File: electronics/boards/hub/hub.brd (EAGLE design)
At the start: 48 x 48 mm, 8 parts, among them J1 GROVE_CONNECTOR2.0_1X4, J2 GROVE_CONNECTOR2.0_1X4, J3 GROVE_CONNECTOR2.0_1X4, J4 GROVE_CONNECTOR2.0_1X4, J5 GROVE_CONNECTOR2.0_1X4, J6 GROVE_CONNECTOR2.0_1X4, J7 GROVE_CONNECTOR2.0_1X4, J8 GROVE_CONNECTOR2.0_1X4

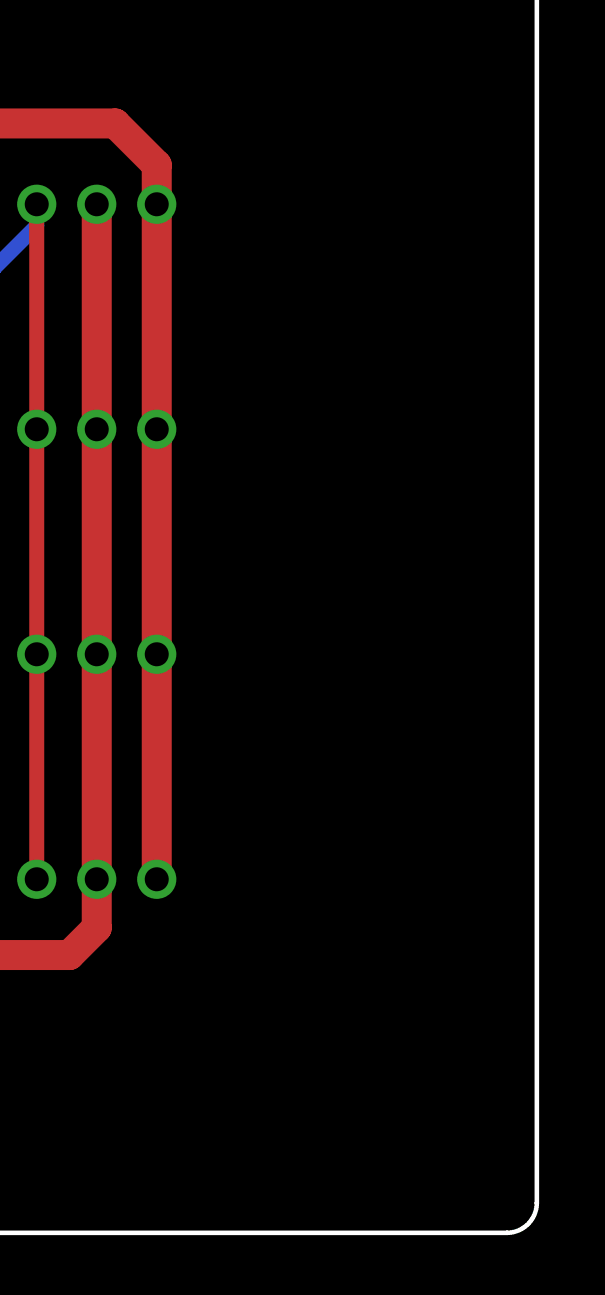
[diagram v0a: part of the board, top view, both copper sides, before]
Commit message: Logo hinzugefügt
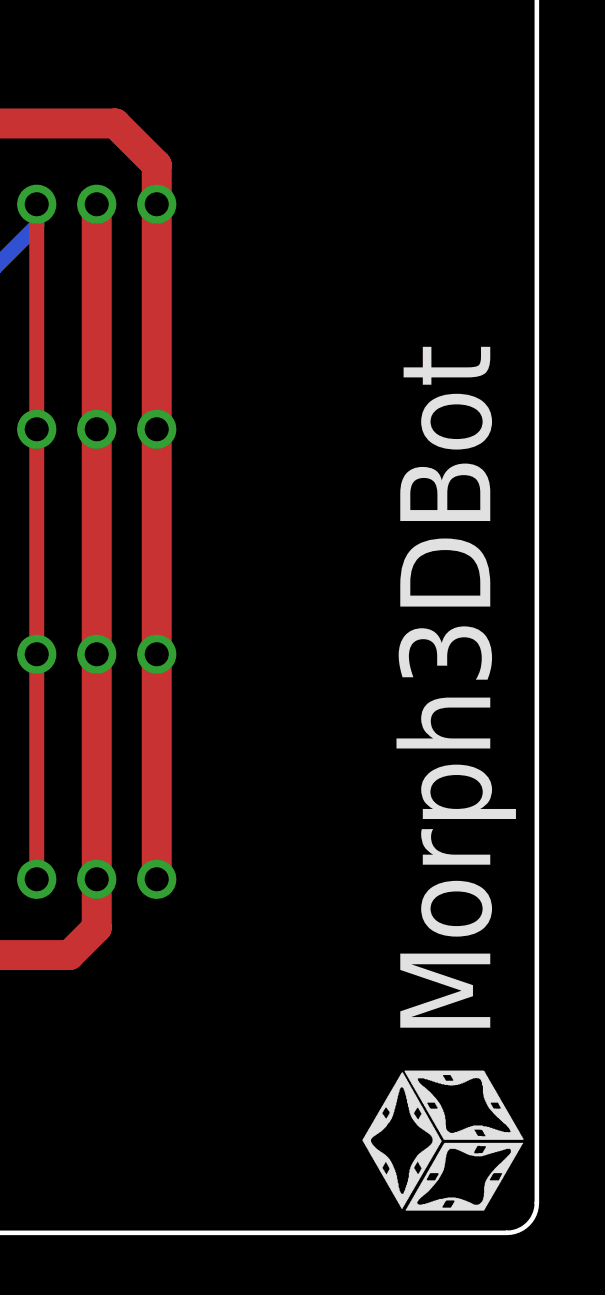
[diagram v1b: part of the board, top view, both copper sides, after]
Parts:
- added U$1: LOGO_MORPHBOT5MM, topo-eng:LOGO_MORPHBOT
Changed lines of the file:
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@@
 <layer number="104" name="Name" color="7" fill="1" visible="no" active="yes"/>
 <layer number="116" name="Patch_BOT" color="9" fill="4" visible="no" active="yes"/>
+<layer number="120" name="brd_placement_notes" color="7" fill="1" visible="yes" active="yes"/>
 <layer number="121" name="_tsilk" color="7" fill="1" visible="no" active="yes"/>
 <layer number="122" name="_bsilk" color="7" fill="1" visible="no" active="yes"/>
+<layer number="144" name="DrillLegend" color="7" fill="1" visible="yes" active="yes"/>
+<layer number="145" name="DrillLegend_01-16" color="7" fill="1" visible="yes" active="yes"/>
+<layer number="146" name="DrillLegend_01-20" color="7" fill="1" visible="yes" active="yes"/>
 <layer number="151" name="HeatSink" color="14" fill="1" visible="no" active="no"/>
+<layer number="198" name="BMP198" color="7" fill="1" visible="yes" active="yes"/>
+<layer number="199" name="Contour" color="7" fill="1" visible="yes" active="yes"/>
 <layer number="200" name="200bmp" color="1" fill="10" visible="no" active="no"/>
 <layer number="201" name="201bmp" color="2" fill="1" visible="no" active="no"/>
@@
 <layer number="207" name="207bmp" color="15" fill="10" visible="no" active="no"/>
 <layer number="208" name="208bmp" color="9" fill="10" visible="no" active="yes"/>
+<layer number="209" name="Route9Document" color="7" fill="1" visible="yes" active="yes"/>
+<layer number="210" name="Route10Document" color="7" fill="1" visible="yes" active="yes"/>
+<layer number="211" name="Route11Document" color="7" fill="1" visible="yes" active="yes"/>
+<layer number="212" name="Route12Document" color="7" fill="1" visible="yes" active="yes"/>
+<layer number="213" name="Route13Document" color="7" fill="1" visible="yes" active="yes"/>
+<layer number="214" name="Route14Document" color="7" fill="1" visible="yes" active="yes"/>
+<layer number="215" name="Route15Document" color="7" fill="1" visible="yes" active="yes"/>
+<layer number="216" name="BottomDocument" color="7" fill="1" visible="yes" active="yes"/>
+<layer number="220" name="DimensionDocument" color="7" fill="1" visible="yes" active="yes"/>
+<layer number="221" name="tPlaceDocument" color="7" fill="1" visible="yes" active="yes"/>
+<layer number="222" name="bPlaceDocument" color="7" fill="1" visible="yes" active="yes"/>
+<layer number="225" name="tNamesDocument" color="7" fill="1" visible="yes" active="yes"/>
+<layer number="226" name="bNamesDocument" color="7" fill="1" visible="yes" active="yes"/>
+<layer number="227" name="tValuesDocument" color="7" fill="1" visible="yes" active="yes"/>
+<layer number="228" name="bValuesDocument" color="7" fill="1" visible="yes" active="yes"/>
+<layer number="229" name="tStopDocument" color="7" fill="1" visible="yes" active="yes"/>
+<layer number="230" name="bStopDocument" color="7" fill="1" visible="yes" active="yes"/>
+<layer number="231" name="tCreamDocument" color="7" fill="1" visible="yes" active="yes"/>
+<layer number="232" name="bCreamDocument" color="7" fill="1" visible="yes" active="yes"/>
+<layer number="233" name="tFinishDocument" color="7" fill="1" visible="yes" active="yes"/>
+<layer number="234" name="bFinishDocument" color="7" fill="1" visible="yes" active="yes"/>
+<layer number="235" name="tGlueDocument" color="7" fill="1" visible="yes" active="yes"/>
+<layer number="236" name="bGlueDocument" color="7" fill="1" visible="yes" active="yes"/>
+<layer number="244" name="DrillsDocument" color="7" fill="1" visible="yes" active="yes"/>
+<layer number="245" name="HolesDocument" color="7" fill="1" visible="yes" active="yes"/>
+<layer number="246" name="MillingDocument" color="7" fill="1" visible="yes" active="yes"/>
+<layer number="247" name="MeasuresDocument" color="7" fill="1" visible="yes" active="yes"/>
 <layer number="250" name="Descript" color="3" fill="1" visible="no" active="no"/>
 <layer number="251" name="SMDround" color="12" fill="11" visible="no" active="no"/>
@@
 <attribute name="NAME" x="10.892778125" y="24.20470625" size="0.8128" layer="26" font="vector" ratio="10" rot="MR180"/>
 </element>
+<element name="U$1" library="topo-eng" library_urn="urn:adsk.eagle:library:6646478" package="LOGO_MORPHBOT" value="LOGO_MORPHBOT5MM" x="47.657946875" y="0.4947" smashed="yes" rot="R90"/>
 </elements>
 <signals>
@@
 </drawing>
 <compatibility>
+<note version="8.2" severity="warning">
+Since Version 8.2, EAGLE supports online libraries. The ids
+of those online libraries will not be understood (or retained)
+with this version.
+</note>
 <note version="8.3" severity="warning">
 Since Version 8.3, EAGLE supports URNs for individual library

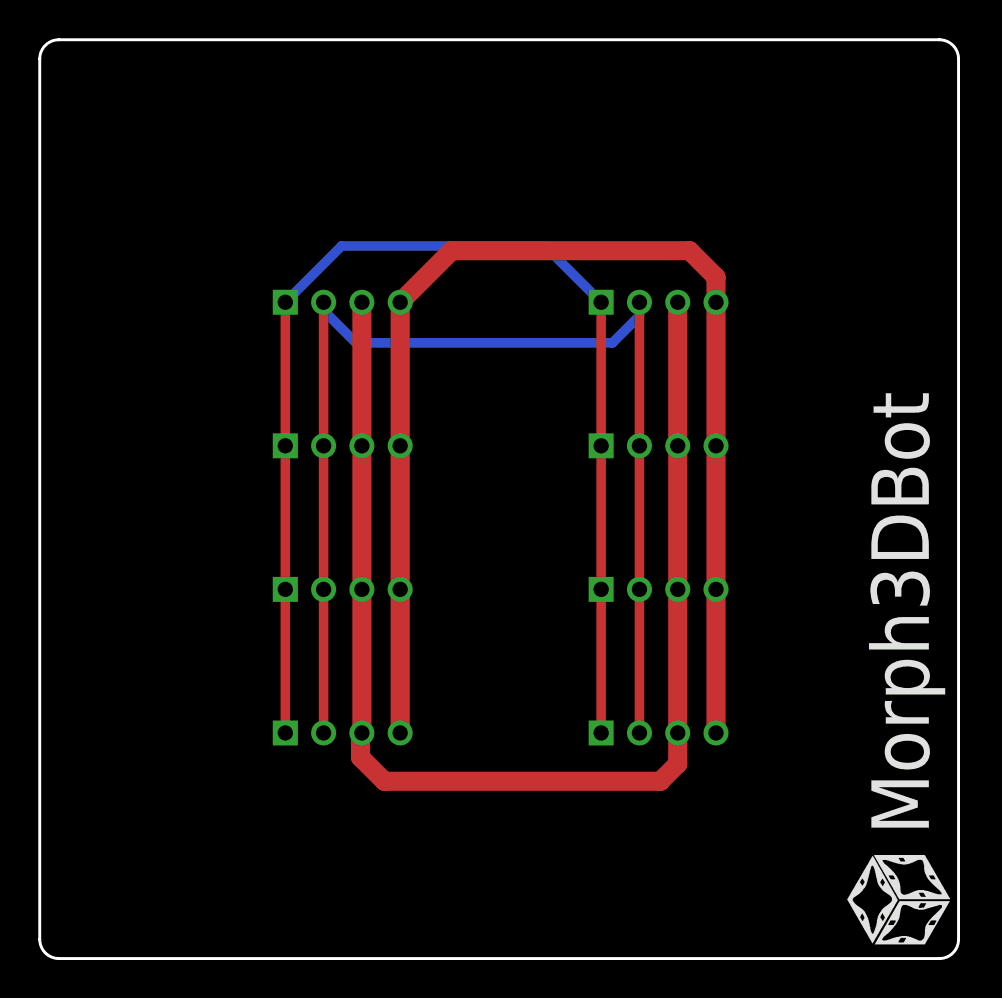
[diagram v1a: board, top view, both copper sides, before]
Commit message: Fiducials eingefügt
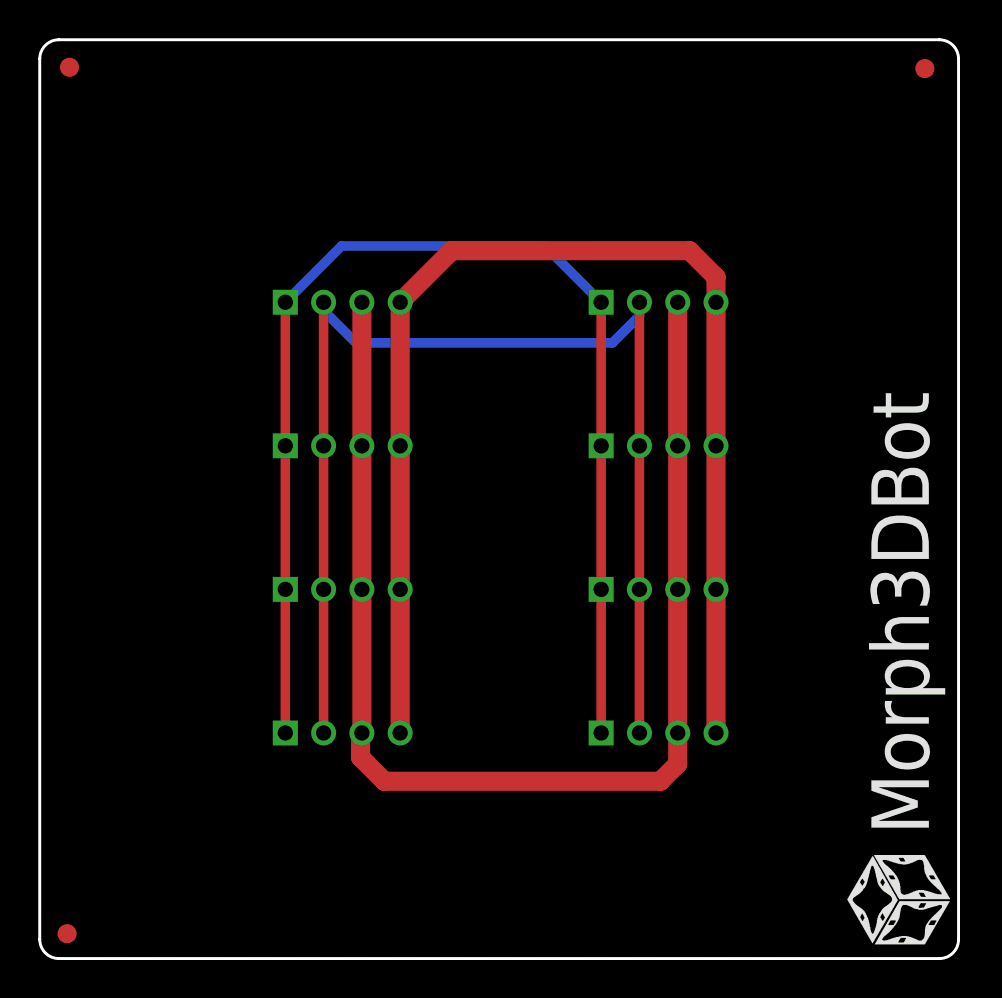
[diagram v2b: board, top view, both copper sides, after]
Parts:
- added FID1, FID2, FID3: OPEN-PNP-FIDUCIAL, topo-eng:OPEN-PNP-FIDUCIAL
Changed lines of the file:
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@@
 </element>
 <element name="U$1" library="topo-eng" library_urn="urn:adsk.eagle:library:6646478" package="LOGO_MORPHBOT" value="LOGO_MORPHBOT5MM" x="47.657946875" y="0.4947" smashed="yes" rot="R90"/>
+<element name="FID1" library="topo-eng" library_urn="urn:adsk.eagle:library:6646478" package="OPEN-PNP-FIDUCIAL" value="OPEN-PNP-FIDUCIAL" x="1.42945625" y="1.296825" smashed="yes"/>
+<element name="FID2" library="topo-eng" library_urn="urn:adsk.eagle:library:6646478" package="OPEN-PNP-FIDUCIAL" value="OPEN-PNP-FIDUCIAL" x="1.5574125" y="46.56078125" smashed="yes"/>
+<element name="FID3" library="topo-eng" library_urn="urn:adsk.eagle:library:6646478" package="OPEN-PNP-FIDUCIAL" value="OPEN-PNP-FIDUCIAL" x="46.239703125" y="46.492925" smashed="yes"/>
 </elements>
 <signals>
